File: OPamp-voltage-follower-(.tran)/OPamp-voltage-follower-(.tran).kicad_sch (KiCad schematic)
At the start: 4 parts, among them U1 LM741

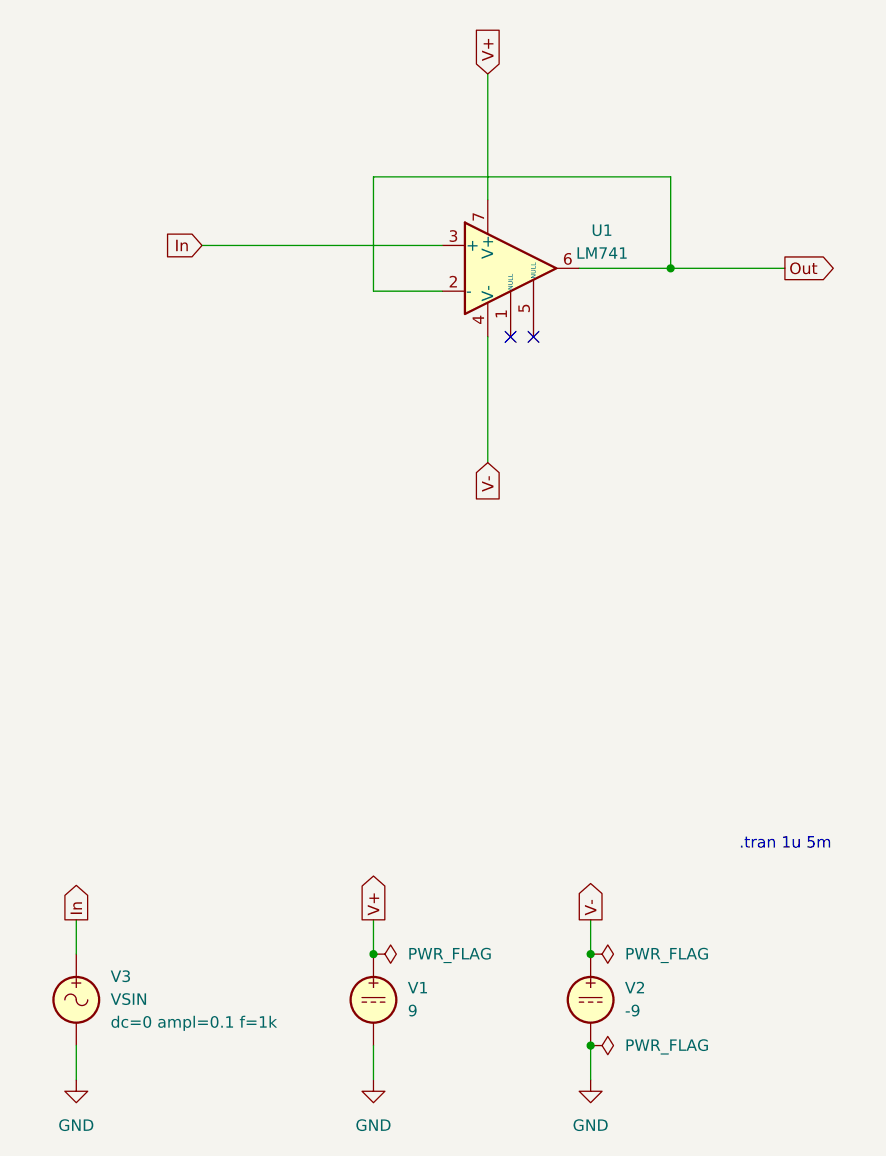
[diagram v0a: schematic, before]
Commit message: Updated all schematics and prepared for KiCad 8.0
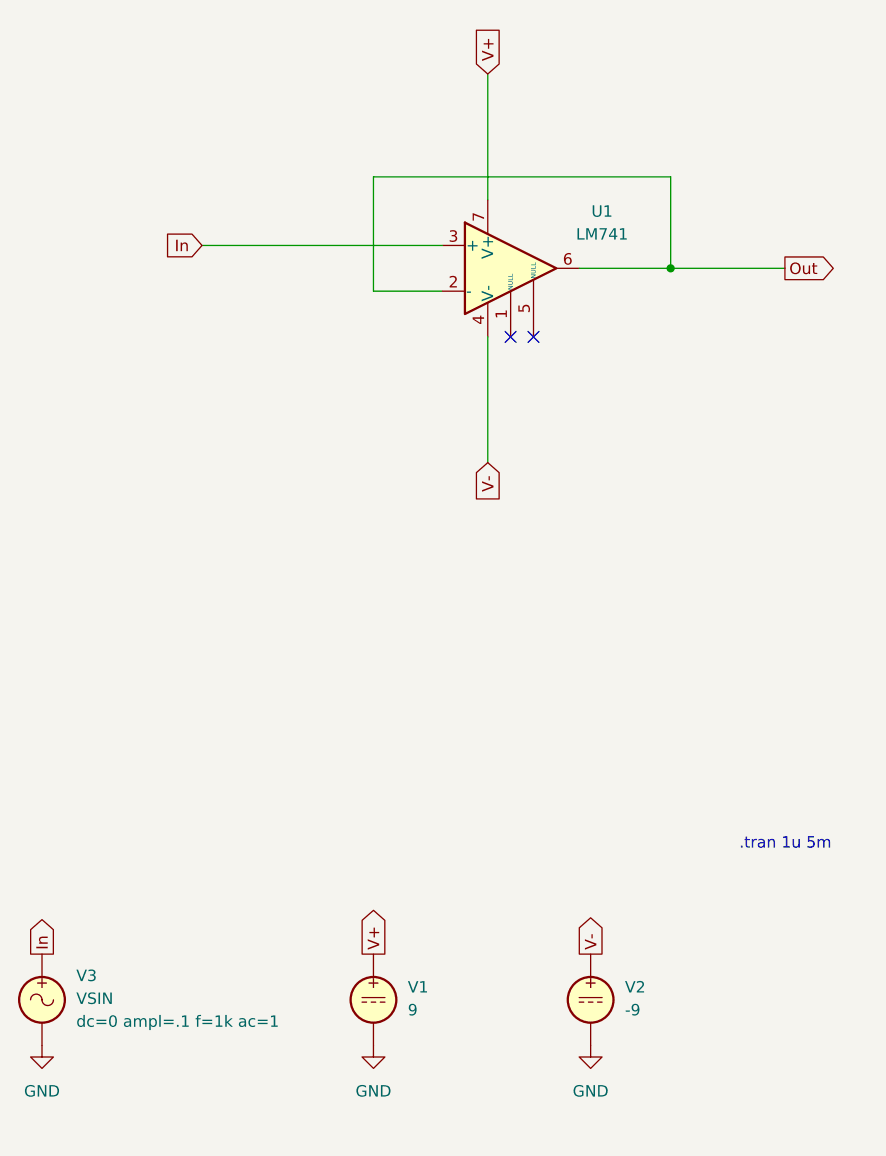
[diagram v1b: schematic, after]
